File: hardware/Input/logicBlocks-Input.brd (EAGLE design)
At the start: 10.2 x 16.5 mm, 12 parts

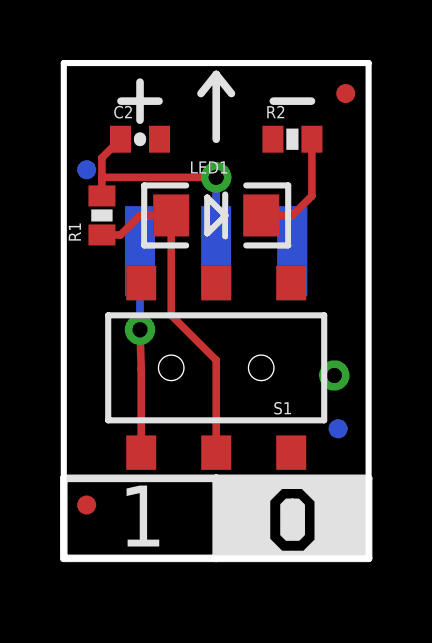
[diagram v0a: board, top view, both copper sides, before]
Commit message: v12 of all boards -- Male headers w/ posts
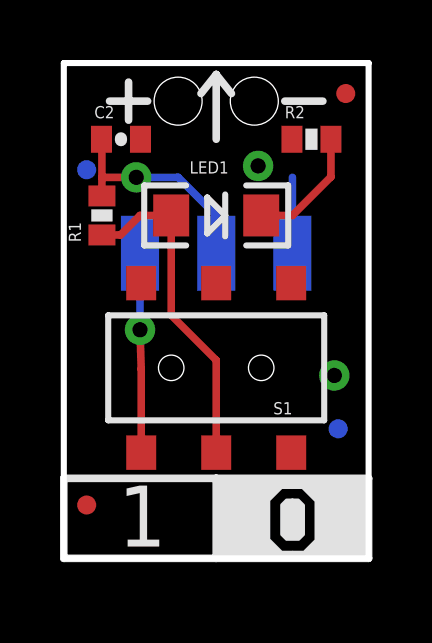
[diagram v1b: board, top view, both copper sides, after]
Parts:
- removed JP1: (no value), SparkFun:1X03-SMD-MALE
- added JP7: (no value), SparkFun-Connectors:1X03_SMD_RA_MALE_POST
- moved R2 0.64 mm to (8.26, 14.0)
- moved C2 0.64 mm to (1.91, 14.0)
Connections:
- net GND: now also JP7.3; no longer JP1.3
- net N$1: now also JP7.2; no longer JP1.2
- net VCC: now also JP7.1; no longer JP1.1
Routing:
- net GND: track 0.00 -> 2.53 mm, vias 1 -> 2
- net N$1: track 8.42 -> 7.49 mm
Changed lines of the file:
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@@
 <layer number="50" name="dxf" color="7" fill="1" visible="no" active="yes"/>
 <layer number="51" name="tDocu" color="6" fill="1" visible="yes" active="yes"/>
-<layer number="52" name="bDocu" color="7" fill="1" visible="yes" active="yes"/>
+<layer number="52" name="bDocu" color="7" fill="1" visible="no" active="yes"/>
 <layer number="53" name="tGND_GNDA" color="7" fill="9" visible="no" active="no"/>
 <layer number="54" name="bGND_GNDA" color="1" fill="9" visible="no" active="no"/>
@@
 <layer number="144" name="Drill_legend" color="7" fill="1" visible="no" active="yes"/>
 <layer number="151" name="HeatSink" color="7" fill="1" visible="no" active="yes"/>
+<layer number="199" name="Contour" color="7" fill="1" visible="no" active="yes"/>
 <layer number="200" name="200bmp" color="1" fill="10" visible="no" active="yes"/>
 <layer number="201" name="201bmp" color="2" fill="10" visible="no" active="yes"/>
@@
 <wire x1="10.16" y1="16.51" x2="10.16" y2="0" width="0.2032" layer="20"/>
 <wire x1="10.16" y1="0" x2="0" y2="0" width="0.2032" layer="20"/>
-<wire x1="3.175" y1="15.24" x2="1.905" y2="15.24" width="0.254" layer="21"/>
-<wire x1="8.255" y1="15.24" x2="6.985" y2="15.24" width="0.254" layer="21"/>
-<wire x1="2.54" y1="15.875" x2="2.54" y2="14.605" width="0.254" layer="21"/>
+<wire x1="2.794" y1="15.24" x2="1.524" y2="15.24" width="0.254" layer="21"/>
+<wire x1="8.636" y1="15.24" x2="7.366" y2="15.24" width="0.254" layer="21"/>
+<wire x1="2.159" y1="15.875" x2="2.159" y2="14.605" width="0.254" layer="21"/>
 <wire x1="5.08" y1="2.667" x2="10.16" y2="2.667" width="0.254" layer="21"/>
 <wire x1="10.16" y1="2.667" x2="10.16" y2="0" width="0.254" layer="21"/>
@@
 <element name="S1" library="SparkFun" package="AYZ0202" value="" x="5.08" y="6.35" rot="R180"/>
 <element name="LED1" library="SparkFun" package="LED-1206" value="GREEN" x="5.08" y="11.43"/>
-<element name="R2" library="SparkFun" package="0402-RES" value="200" x="7.62" y="13.97"/>
-<element name="JP1" library="SparkFun" package="1X03-SMD-MALE" value="" x="5.08" y="15.24" rot="MR180"/>
+<element name="R2" library="SparkFun" package="0402-RES" value="200" x="8.255" y="13.97"/>
 <element name="JP2" library="SparkFun" package="SFE-LOGO-FLAME" value="LOGO-SFESK" x="9.271" y="0.508" rot="MR0"/>
 <element name="U$2" library="SparkFun" package="CREATIVE_COMMONS" value="CREATIVE_COMMONS" x="10.16" y="-2.54" rot="MR0"/>
 <element name="R1" library="SparkFun" package="0402-RES" value="499k" x="1.27" y="11.43" rot="R90"/>
-<element name="C2" library="SparkFun" package="0402-CAP" value="1uF" x="2.54" y="13.97"/>
+<element name="C2" library="SparkFun" package="0402-CAP" value="1uF" x="1.905" y="13.97"/>
 <element name="JP3" library="SparkFun" package="MICRO-FIDUCIAL" value="FIDUCIALUFIDUCIAL" x="9.144" y="4.318" rot="MR0"/>
 <element name="JP4" library="SparkFun" package="MICRO-FIDUCIAL" value="FIDUCIALUFIDUCIAL" x="0.762" y="12.954" rot="MR0"/>
 <element name="JP5" library="SparkFun" package="MICRO-FIDUCIAL" value="FIDUCIALUFIDUCIAL" x="0.762" y="1.778"/>
 <element name="JP6" library="SparkFun" package="MICRO-FIDUCIAL" value="FIDUCIALUFIDUCIAL" x="9.398" y="15.494"/>
+<element name="JP7" library="SparkFun-Connectors" package="1X03_SMD_RA_MALE_POST" value="" x="5.08" y="15.24" rot="MR180"/>
 </elements>
 <signals>
 <signal name="VCC">
 <contactref element="S1" pad="3"/>
-<contactref element="JP1" pad="1"/>
 <wire x1="2.58" y1="3.525" x2="2.58" y2="6.31" width="0.254" layer="1"/>
 <wire x1="2.58" y1="6.31" x2="2.54" y2="7.62" width="0.254" layer="1"/>
-<wire x1="2.54" y1="7.62" x2="2.54" y2="10.24" width="0.254" layer="16"/>
 <via x="2.54" y="7.62" extent="1-16" drill="0.508"/>
+<contactref element="JP7" pad="1"/>
+<wire x1="2.54" y1="10.17" x2="2.54" y2="7.62" width="0.254" layer="16"/>
 </signal>
 <signal name="GND">
@@
 <contactref element="S1" pad="1"/>
 <contactref element="C2" pad="2"/>
-<contactref element="JP1" pad="3"/>
 <via x="9.017" y="6.096" extent="1-16" drill="0.508"/>
 <polygon width="0.254" layer="16" isolate="0.3048">
@@
 <vertex x="0" y="16.51"/>
 </polygon>
+<contactref element="JP7" pad="3"/>
+<wire x1="7.62" y1="10.17" x2="7.62" y2="12.7" width="0.254" layer="16"/>
+<via x="6.477" y="13.081" extent="1-16" drill="0.508"/>
 </signal>
 <signal name="N$2">
@@
 <contactref element="LED1" pad="C"/>
 <wire x1="6.58" y1="11.43" x2="7.62" y2="11.43" width="0.254" layer="1"/>
-<wire x1="8.27" y1="12.08" x2="8.27" y2="13.97" width="0.254" layer="1"/>
-<wire x1="7.62" y1="11.43" x2="8.27" y2="12.08" width="0.254" layer="1"/>
+<wire x1="7.62" y1="11.43" x2="8.905" y2="12.715" width="0.254" layer="1"/>
+<wire x1="8.905" y1="13.97" x2="8.905" y2="12.715" width="0.254" layer="1"/>
 </signal>
 <signal name="N$1">
 <contactref element="R1" pad="2"/>
 <contactref element="C2" pad="1"/>
-<contactref element="JP1" pad="2"/>
-<wire x1="5.08" y1="12.7" x2="5.08" y2="10.24" width="0.254" layer="16"/>
 <wire x1="1.27" y1="12.08" x2="1.27" y2="12.7" width="0.254" layer="1"/>
-<wire x1="1.27" y1="12.7" x2="1.27" y2="13.35" width="0.254" layer="1"/>
-<wire x1="1.27" y1="13.35" x2="1.89" y2="13.97" width="0.254" layer="1"/>
-<wire x1="1.27" y1="12.7" x2="5.08" y2="12.7" width="0.254" layer="1"/>
-<via x="5.08" y="12.7" extent="1-16" drill="0.508"/>
+<wire x1="1.27" y1="12.7" x2="1.27" y2="13.955" width="0.254" layer="1"/>
+<wire x1="1.27" y1="12.7" x2="2.413" y2="12.7" width="0.254" layer="1"/>
+<via x="2.413" y="12.7" extent="1-16" drill="0.508"/>
+<contactref element="JP7" pad="2"/>
+<wire x1="5.08" y1="10.17" x2="5.08" y2="11.43" width="0.254" layer="16"/>
+<wire x1="5.08" y1="11.43" x2="3.81" y2="12.7" width="0.254" layer="16"/>
+<wire x1="3.81" y1="12.7" x2="2.413" y2="12.7" width="0.254" layer="16"/>
+<wire x1="1.27" y1="13.955" x2="1.255" y2="13.97" width="0.254" layer="1"/>
 </signal>
 </signals>
